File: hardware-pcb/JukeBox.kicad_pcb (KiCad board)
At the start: 2 copper layers, 90 x 90 mm, 74 parts, among them J1 USB4105-GF-A, J2 Conn_01x03, J3 Conn_01x04, J4 Conn_01x08, J5 Conn_01x01, J6 Conn_01x03, J7 Conn_01x03, J8 Conn_01x01, SW1 SW_SPST, SW10 SW_SPST, SW11 SW_SPST, SW12 SW_SPST, SW2 SW_SPST, SW3 SW_SPST, SW4 SW_SPST, SW5 SW_SPST, SW6 SW_SPST, SW7 SW_SPST, SW8 SW_SPST, SW9 SW_SPST, U1 NCP1117-3.3_SOT223, U2 W25Q128JVS, U3 RP2040, Y1 ABLS-12.000MHZ-B4-T

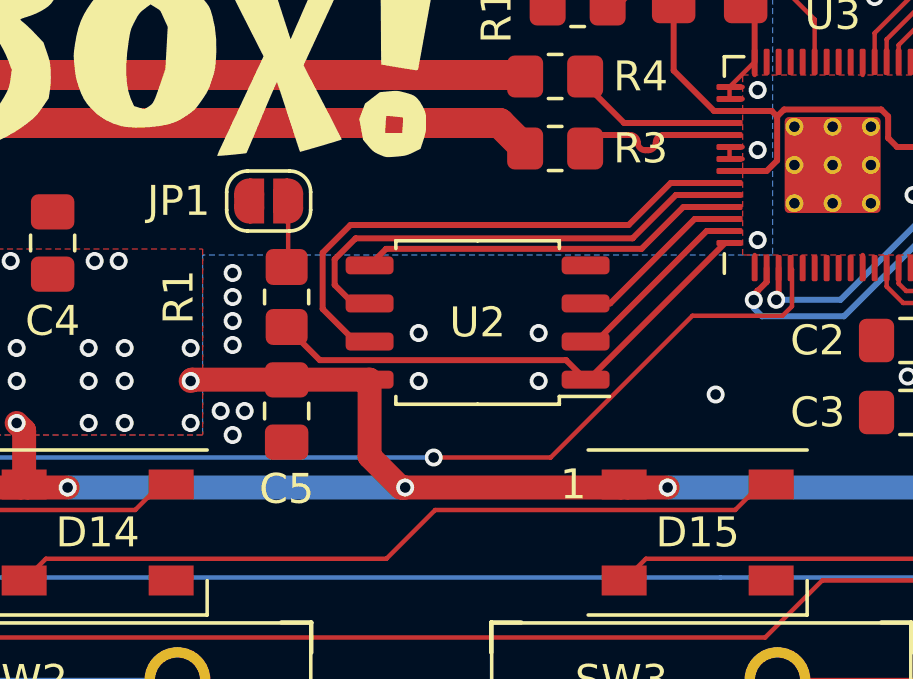
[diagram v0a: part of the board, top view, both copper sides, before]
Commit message: add more pillars for keyboard frame support, fix footprint for firmware chip
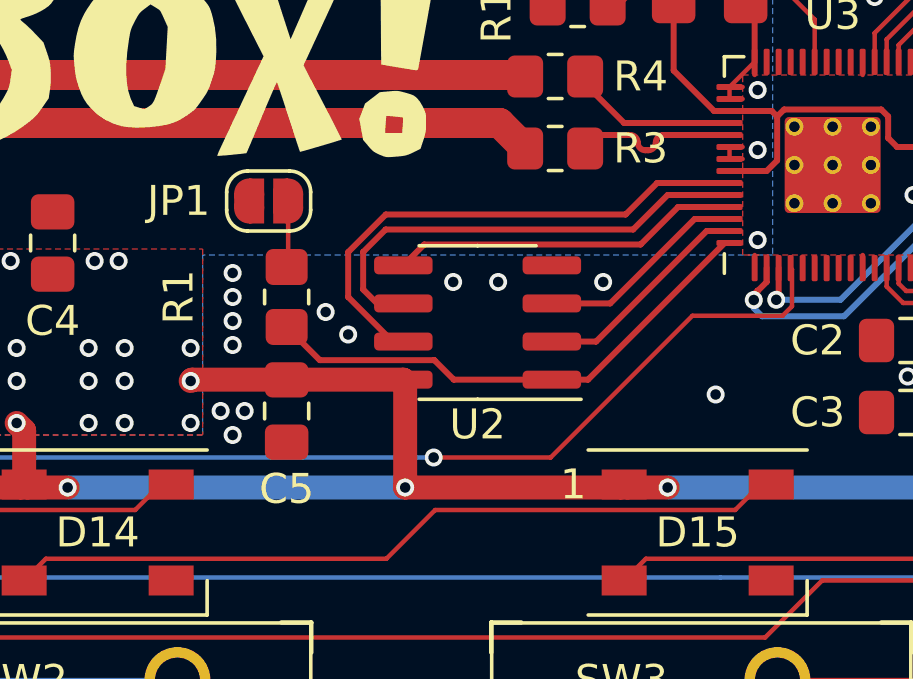
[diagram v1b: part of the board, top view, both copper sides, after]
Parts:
- U2: footprint Package_SO:SOIC-8_5.23x5.23mm_P1.27mm -> Package_SO:SOIC-8_3.9x4.9mm_P1.27mm
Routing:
- net /QSPI_SD2: track 5.96 -> 7.09 mm
- net /QSPI_SD1: track 6.32 -> 7.45 mm
- net /QSPI_SD0: track 12.8 -> 11.7 mm
- net /QSPI_SD3: track 18.4 -> 17.6 mm
- net +3V3: track 248.9 -> 249.4 mm
- net /QSPI_SCLK: track 16.3 -> 15.8 mm
- net GND: vias 52 -> 53

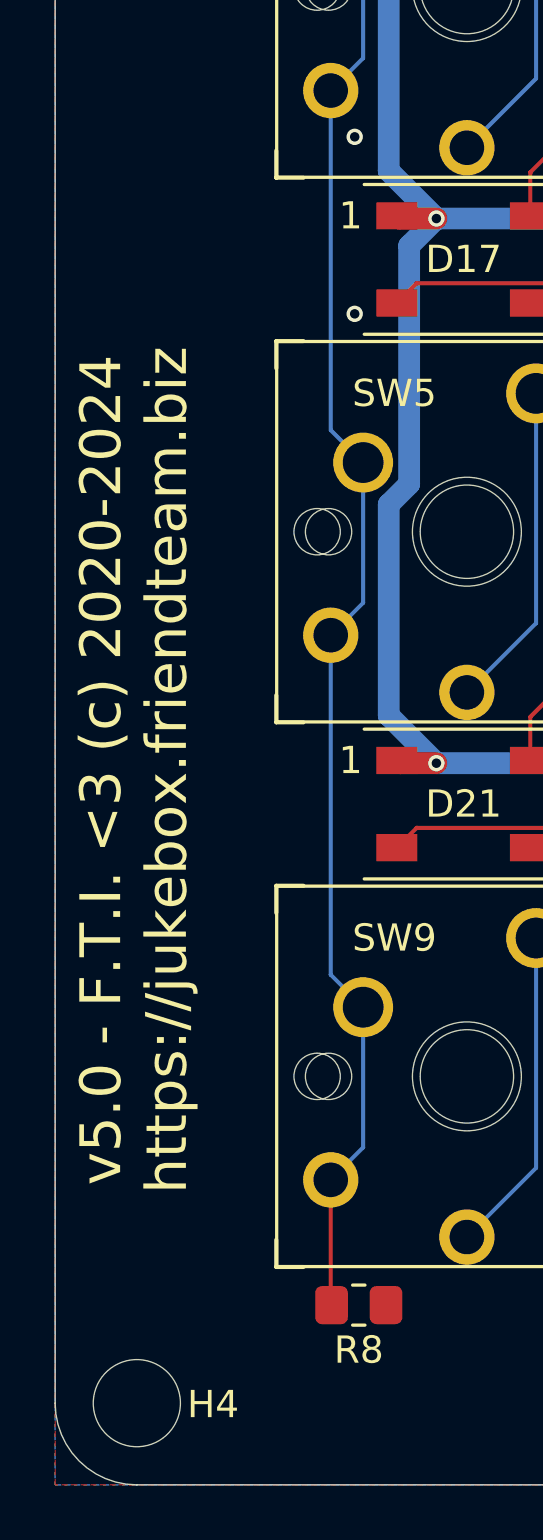
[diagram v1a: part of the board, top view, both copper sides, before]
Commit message: (temporarily) swap row and col on keyboard, add notes for v5.1
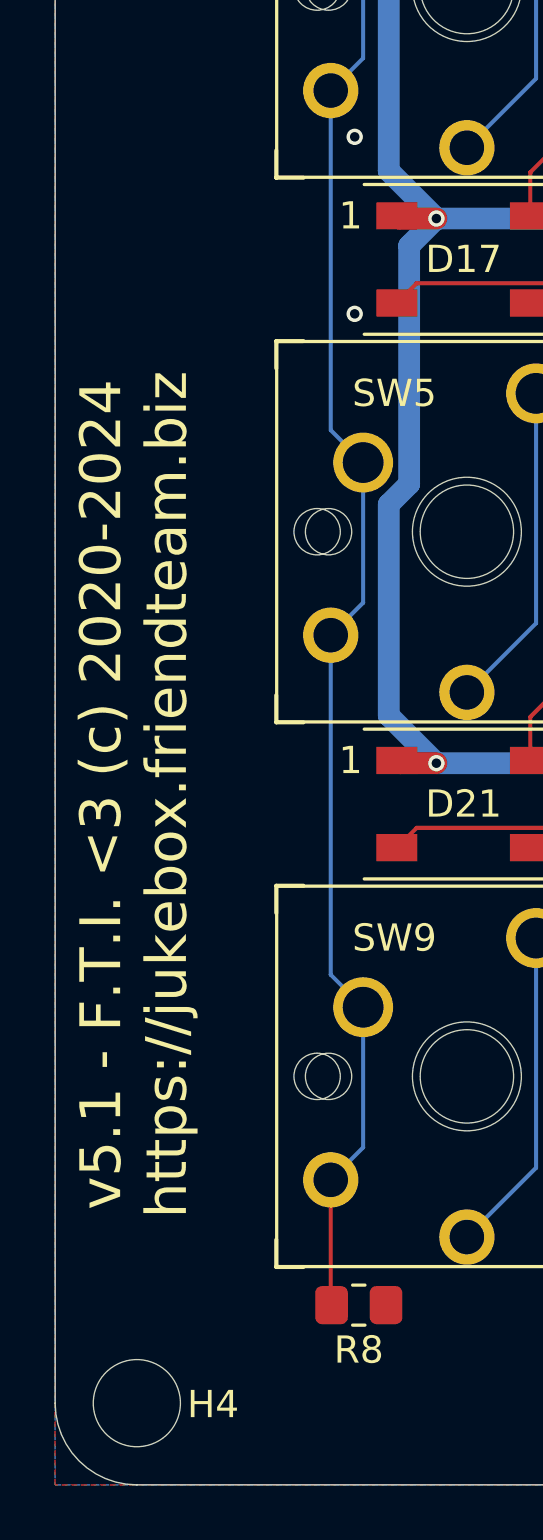
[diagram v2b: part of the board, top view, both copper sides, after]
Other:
- board text added: "v5.1 - F.T.I. <3 (c) 2020-2024 https://jukebox.friendteam.biz"
- board text removed: "v5.0 - F.T.I. <3 (c) 2020-2024 https://jukebox.friendteam.biz"
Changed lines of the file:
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@@
   (gr_line (start 172.49 196.85) (end 88.49 196.85) (layer "Edge.Cuts") (width 0.05))
   (gr_line (start 175.49 109.85) (end 175.49 193.85) (layer "Edge.Cuts") (width 0.05))
-  (gr_text "v5.0 - F.T.I. <3 (c) 2020-2024\nhttps://jukebox.friendteam.biz" (at 88.39 170.6 90) (layer "F.SilkS")
+  (gr_text "v5.1 - F.T.I. <3 (c) 2020-2024\nhttps://jukebox.friendteam.biz" (at 88.39 171.5 90) (layer "F.SilkS")
     (effects (font (size 1.5 1.5) (thickness 0.3)))
   )

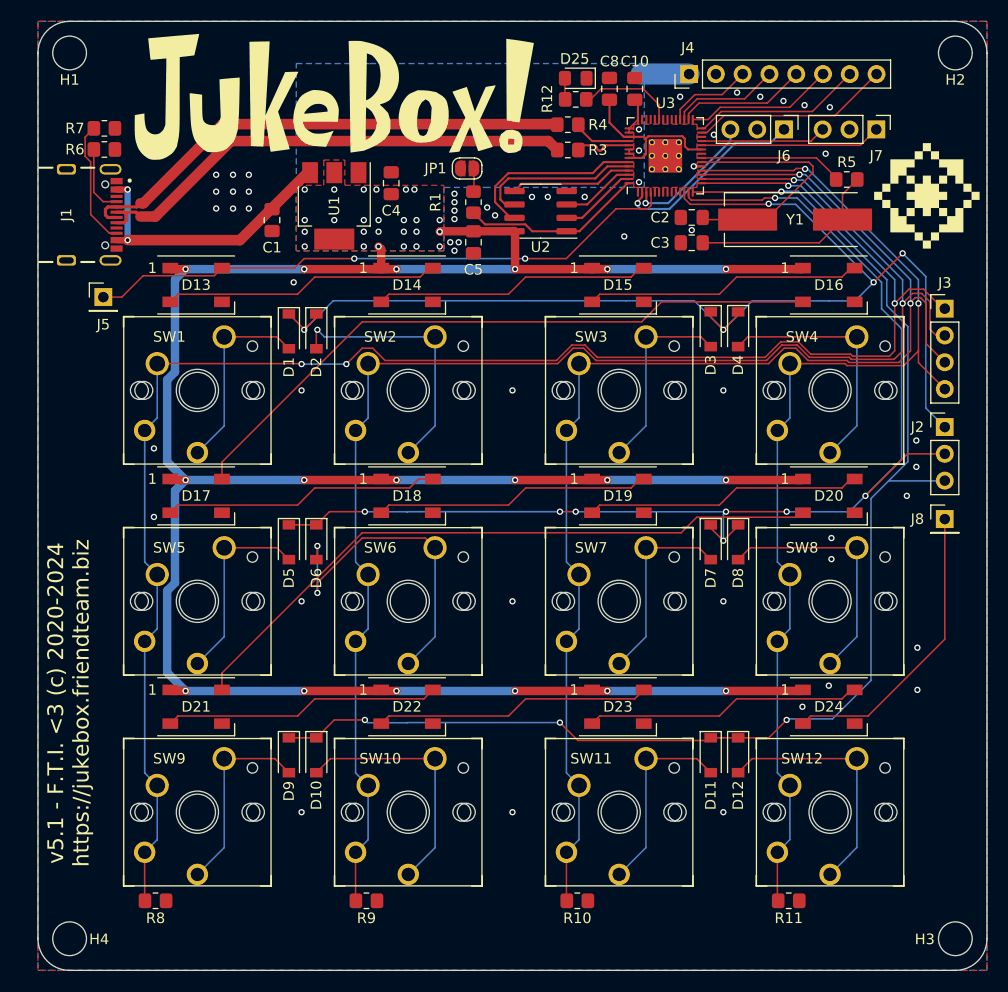
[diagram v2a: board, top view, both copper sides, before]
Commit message: fix keyboard diode direction
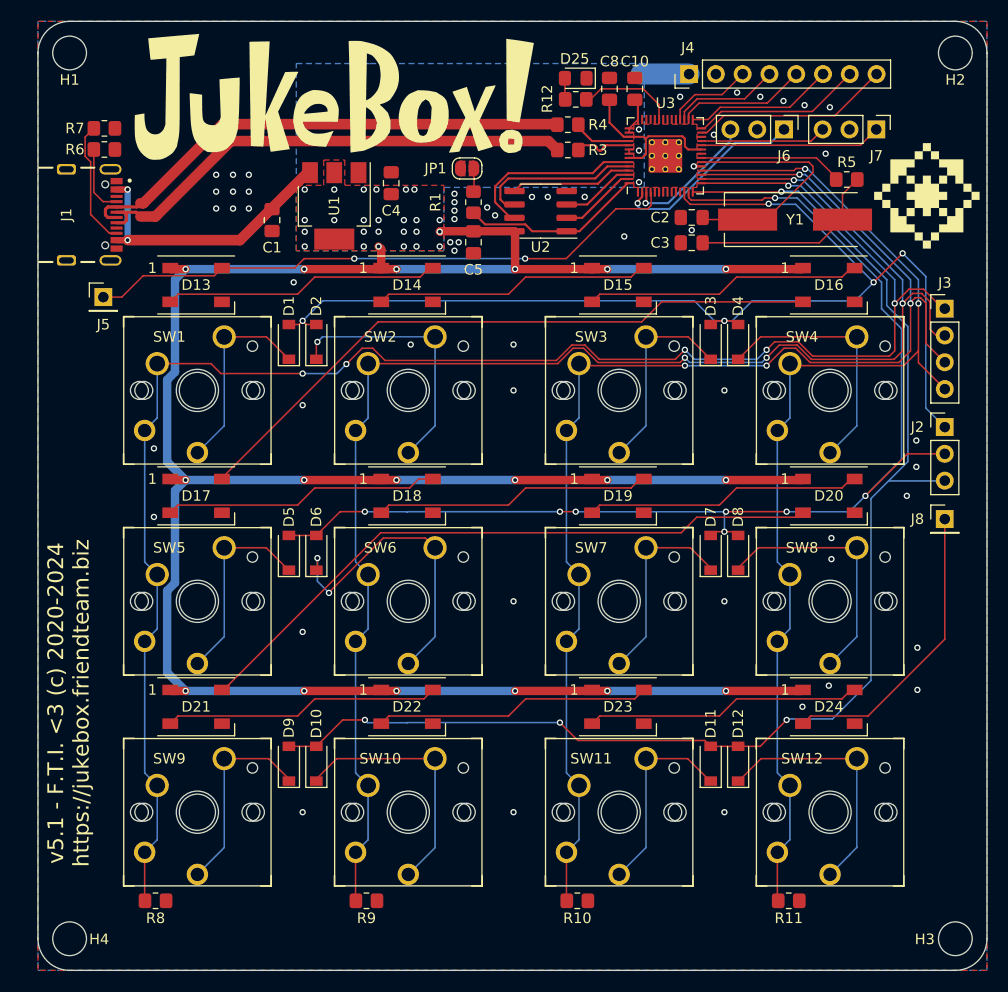
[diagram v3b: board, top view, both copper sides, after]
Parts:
- moved D3 1.20 mm to (149.3, 137.2), turned to 90 degrees
- moved D4 1.20 mm to (151.9, 137.2), turned to 90 degrees
- moved D1 1.00 mm to (109.3, 137.2), turned to 90 degrees
- moved D2 1.00 mm to (111.9, 137.2), turned to 90 degrees
- moved D5 1.00 mm to (109.3, 157.2), turned to 90 degrees
- moved D6 1.00 mm to (111.9, 157.2), turned to 90 degrees
- moved D7 1.00 mm to (149.3, 157.2), turned to 90 degrees
- moved D8 1.00 mm to (151.9, 157.2), turned to 90 degrees
- moved D10 0.80 mm to (111.9, 177.2), turned to 90 degrees
- moved D11 0.80 mm to (149.3, 177.2), turned to 90 degrees
- moved D12 0.80 mm to (151.9, 177.2), turned to 90 degrees
- moved D9 0.80 mm to (109.3, 177.2), turned to 90 degrees
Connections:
- D1 pad 1: /GPIO9 -> Net-(D1-Pad1)
- D1 pad 2: Net-(D1-Pad2) -> /GPIO9
- D10 pad 1: /GPIO11 -> Net-(D10-Pad1)
- D10 pad 2: Net-(D10-Pad2) -> /GPIO11
- D11 pad 1: /GPIO11 -> Net-(D11-Pad1)
- D11 pad 2: Net-(D11-Pad2) -> /GPIO11
- D12 pad 1: /GPIO11 -> Net-(D12-Pad1)
- D12 pad 2: Net-(D12-Pad2) -> /GPIO11
- D2 pad 1: /GPIO9 -> Net-(D2-Pad1)
- D2 pad 2: Net-(D2-Pad2) -> /GPIO9
- D3 pad 1: /GPIO9 -> Net-(D3-Pad1)
- D3 pad 2: Net-(D3-Pad2) -> /GPIO9
- D4 pad 1: /GPIO9 -> Net-(D4-Pad1)
- D4 pad 2: Net-(D4-Pad2) -> /GPIO9
- D5 pad 1: /GPIO10 -> Net-(D5-Pad1)
- D5 pad 2: Net-(D5-Pad2) -> /GPIO10
- D6 pad 1: /GPIO10 -> Net-(D6-Pad1)
- D6 pad 2: Net-(D6-Pad2) -> /GPIO10
- D7 pad 1: /GPIO10 -> Net-(D7-Pad1)
- D7 pad 2: Net-(D7-Pad2) -> /GPIO10
- D8 pad 1: /GPIO10 -> Net-(D8-Pad1)
- D8 pad 2: Net-(D8-Pad2) -> /GPIO10
- D9 pad 1: /GPIO11 -> Net-(D9-Pad1)
- D9 pad 2: Net-(D9-Pad2) -> /GPIO11
- SW1 pad 1: Net-(D1-Pad2) -> Net-(D1-Pad1)
- SW10 pad 1: Net-(D10-Pad2) -> Net-(D10-Pad1)
- SW11 pad 1: Net-(D11-Pad2) -> Net-(D11-Pad1)
- SW12 pad 1: Net-(D12-Pad2) -> Net-(D12-Pad1)
- SW2 pad 1: Net-(D2-Pad2) -> Net-(D2-Pad1)
- SW3 pad 1: Net-(D3-Pad2) -> Net-(D3-Pad1)
- SW4 pad 1: Net-(D4-Pad2) -> Net-(D4-Pad1)
- SW5 pad 1: Net-(D5-Pad2) -> Net-(D5-Pad1)
- SW6 pad 1: Net-(D6-Pad2) -> Net-(D6-Pad1)
- SW7 pad 1: Net-(D7-Pad2) -> Net-(D7-Pad1)
- SW8 pad 1: Net-(D8-Pad2) -> Net-(D8-Pad1)
- SW9 pad 1: Net-(D9-Pad2) -> Net-(D9-Pad1)
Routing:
- net Net-(D6-Pad2): track 32.0 -> 0.00 mm, vias 2 -> 0
- net Net-(D6-Pad1): track 0.00 -> 29.6 mm, vias 0 -> 2
- net Net-(D2-Pad2): track 25.3 -> 0.00 mm, vias 1 -> 0
- net Net-(D2-Pad1): track 0.00 -> 25.1 mm, vias 0 -> 1
- net Net-(D8-Pad1): track 0.00 -> 24.3 mm
- net Net-(D10-Pad1): track 0.00 -> 24.3 mm
- net Net-(D12-Pad1): track 0.00 -> 24.2 mm
- net Net-(D4-Pad1): track 0.00 -> 24.2 mm
- net Net-(D12-Pad2): track 23.8 -> 0.00 mm
- net Net-(D10-Pad2): track 23.8 -> 0.00 mm
- net Net-(D8-Pad2): track 23.8 -> 0.00 mm
- net Net-(D4-Pad2): track 23.7 -> 0.00 mm
- net Net-(D9-Pad1): track 0.00 -> 19.2 mm
- net Net-(D7-Pad1): track 0.00 -> 19.2 mm
- net Net-(D5-Pad1): track 0.00 -> 19.1 mm
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
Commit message: add smaller clock crystal, with adjusted capacitor values
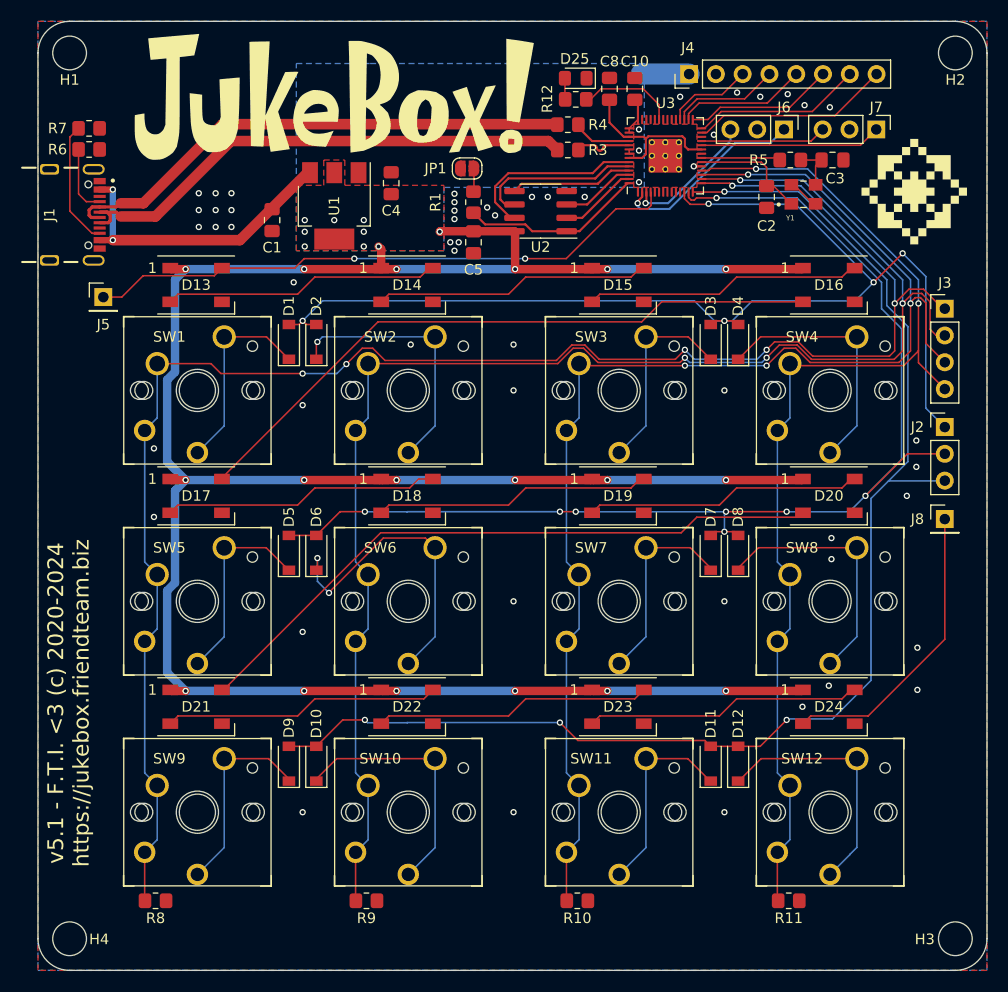
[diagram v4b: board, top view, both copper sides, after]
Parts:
- C2, C3: value 27p -> 32p
- Y1: value ABLS-12.000MHZ-B4-T -> ECS-120-20-33-AEL-TR; footprint RP2040_minimal:Crystal_SMD_HC49-US -> RP2040_minimal:XTAL_ECS-120-20-33-AEL-TR
- moved C3 15.5 mm to (160.8, 120.0)
- moved C2 7.36 mm to (154.6, 123.5), turned to -90 degrees
- moved R5 5.66 mm to (156.8, 120.0)
- moved Y1 2.53 mm to (158.1, 123.2)
- moved J1 1.60 mm to (86.6, 125.2)
- moved R6 1.45 mm to (90.3, 119.0)
- moved R7 1.45 mm to (90.3, 117.0)
- moved G*** 1.26 mm to (168.6, 123.0)
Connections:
- C3 pad 1: Net-(C3-Pad1) -> GND
- C3 pad 2: GND -> Net-(C3-Pad2)
- R5 pad 2: Net-(C3-Pad1) -> Net-(C3-Pad2)
- Y1 pad 2: Net-(C3-Pad1) -> GND
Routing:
- net Net-(C3-Pad1): track 18.6 -> 0.00 mm
- net /XIN: track 23.7 -> 11.2 mm
- net /XOUT: track 13.7 -> 7.50 mm
- net Net-(C3-Pad2): track 0.00 -> 4.55 mm
- net GND: track 8.39 -> 11.4 mm, vias 55 -> 52
- net /USB_D+: track 47.2 -> 49.6 mm
- net VBUS: track 26.8 -> 28.6 mm
- net /USB_D-: track 47.9 -> 49.4 mm
- net +3V3: vias 46 -> 30
